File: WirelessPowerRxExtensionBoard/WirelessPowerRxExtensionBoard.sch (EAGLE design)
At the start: 37 parts, among them Q1 MOSFET-N, Q2 MOSFET-N, Q3 MOSFET-N

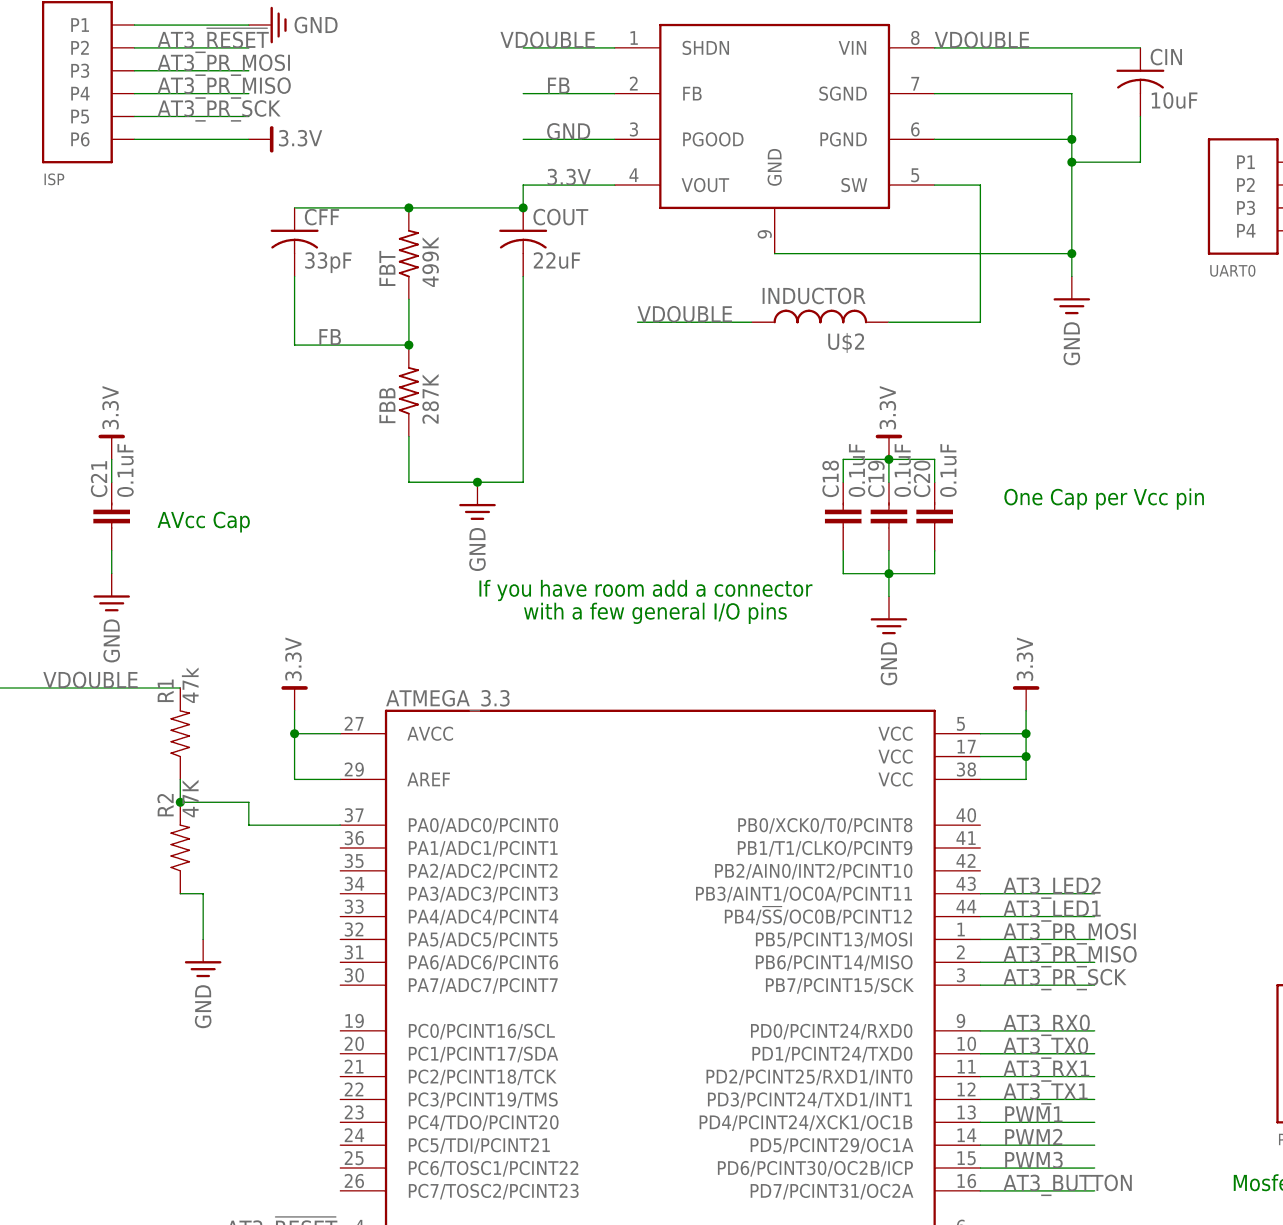
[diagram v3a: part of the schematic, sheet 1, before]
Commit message: Second Rerouting Revision Complete
Extended Ground plane across entire board, switched Voltage regulator
feedback resistors to 0603
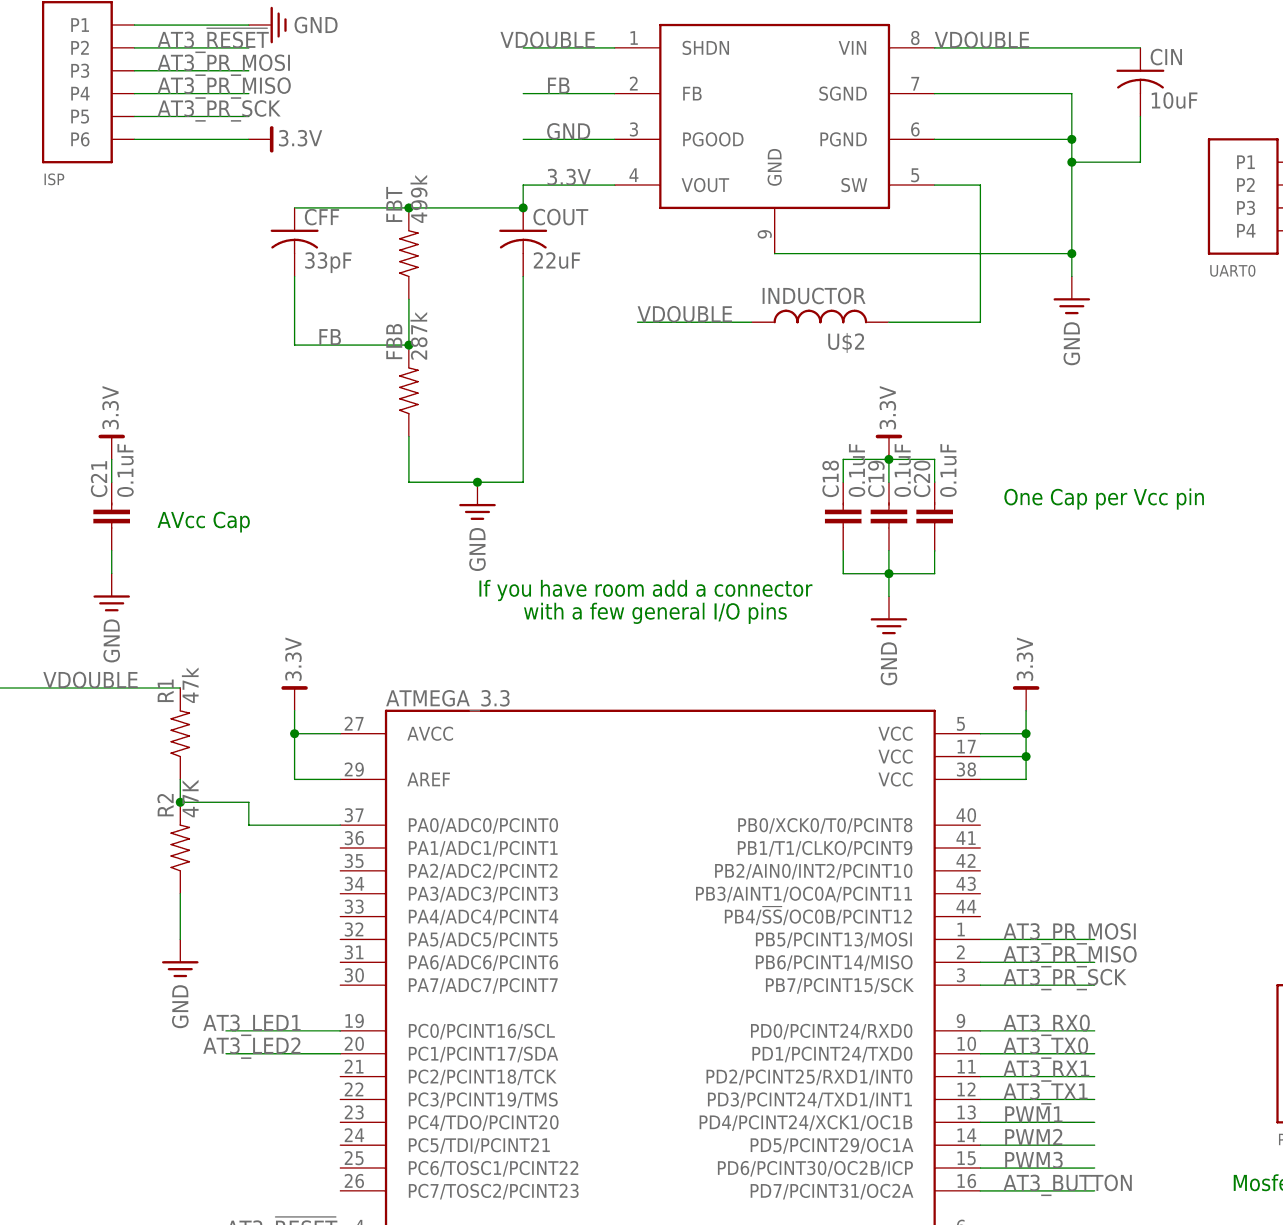
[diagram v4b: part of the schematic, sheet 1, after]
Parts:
- FBB: value 287K -> 287k; device resistor:R-US_M0805 -> carrick:RES0603
- FBT: value 499K -> 499k; device resistor:R-US_M0805 -> carrick:RES0603
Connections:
- net AT3_LED1: now also ATMEGA_3.3.PC0/PCINT16/SCL; no longer ATMEGA_3.3.PB4/!SS!/OC0B/PCINT12
- net AT3_LED2: now also ATMEGA_3.3.PC1/PCINT17/SDA; no longer ATMEGA_3.3.PB3/AINT1/OC0A/PCINT11
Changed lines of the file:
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@@
 <part name="CIN" library="rcl" deviceset="C-US" device="C0805" value="10uF"/>
 <part name="COUT" library="rcl" deviceset="C-US" device="C0805" value="22uF"/>
-<part name="FBT" library="resistor" deviceset="R-US_" device="M0805" value="499K"/>
-<part name="FBB" library="resistor" deviceset="R-US_" device="M0805" value="287K"/>
 <part name="SUPPLY3" library="000_carrick" deviceset="GND" device=""/>
 <part name="CFF" library="rcl" deviceset="C-US" device="C0201" value="33pF"/>
@@
 <part name="R1" library="carrick" deviceset="RES" device="0603" value="47k"/>
 <part name="R2" library="carrick" deviceset="RES" device="0603" value="47K"/>
+<part name="FBT" library="carrick" deviceset="RES" device="0603" value="499k"/>
+<part name="FBB" library="carrick" deviceset="RES" device="0603" value="287k"/>
 </parts>
 <sheets>
@@
 <instance part="CIN" gate="G$1" x="134.62" y="170.18"/>
 <instance part="COUT" gate="G$1" x="66.04" y="152.4"/>
-<instance part="FBT" gate="G$1" x="53.34" y="149.86" rot="R90"/>
-<instance part="FBB" gate="G$1" x="53.34" y="134.62" rot="R90"/>
 <instance part="SUPPLY3" gate="GND" x="60.96" y="121.92"/>
 <instance part="CFF" gate="G$1" x="40.64" y="152.4"/>
 <instance part="U$1" gate="G$1" x="93.98" y="165.1"/>
 <instance part="U$2" gate="G$1" x="99.06" y="142.24" rot="R90"/>
-<instance part="SUPPLY4" gate="GND" x="30.48" y="71.12"/>
+<instance part="SUPPLY4" gate="GND" x="27.94" y="71.12"/>
 <instance part="C1" gate="G$1" x="22.86" y="33.02"/>
 <instance part="C2" gate="G$1" x="22.86" y="17.78"/>
@@
 <instance part="R1" gate="G$1" x="27.94" y="96.52" rot="R90"/>
 <instance part="R2" gate="G$1" x="27.94" y="83.82" rot="R90"/>
+<instance part="FBT" gate="G$1" x="53.34" y="149.86" rot="R90"/>
+<instance part="FBB" gate="G$1" x="53.34" y="134.62" rot="R90"/>
 </instances>
 <busses>
@@
 <pinref part="COUT" gate="G$1" pin="2"/>
 <wire x1="66.04" y1="147.32" x2="66.04" y2="124.46" width="0.1524" layer="91"/>
-<pinref part="FBB" gate="G$1" pin="1"/>
 <wire x1="66.04" y1="124.46" x2="60.96" y2="124.46" width="0.1524" layer="91"/>
 <wire x1="60.96" y1="124.46" x2="53.34" y2="124.46" width="0.1524" layer="91"/>
@@
 <pinref part="SUPPLY3" gate="GND" pin="GND"/>
 <junction x="60.96" y="124.46"/>
+<pinref part="FBB" gate="G$1" pin="1"/>
 </segment>
 <segment>
 <pinref part="SUPPLY4" gate="GND" pin="GND"/>
 <pinref part="R2" gate="G$1" pin="1"/>
-<wire x1="27.94" y1="78.74" x2="30.48" y2="78.74" width="0.1524" layer="91"/>
-<wire x1="30.48" y1="78.74" x2="30.48" y2="73.66" width="0.1524" layer="91"/>
+<wire x1="27.94" y1="73.66" x2="27.94" y2="78.74" width="0.1524" layer="91"/>
 </segment>
 </net>
@@
 <pinref part="COUT" gate="G$1" pin="1"/>
 <wire x1="66.04" y1="157.48" x2="66.04" y2="154.94" width="0.1524" layer="91"/>
-<pinref part="FBT" gate="G$1" pin="2"/>
-<wire x1="66.04" y1="154.94" x2="53.34" y2="154.94" width="0.1524" layer="91"/>
 <junction x="66.04" y="154.94"/>
 <pinref part="CFF" gate="G$1" pin="1"/>
+<wire x1="66.04" y1="154.94" x2="53.34" y2="154.94" width="0.1524" layer="91"/>
+<pinref part="U$1" gate="G$1" pin="VOUT"/>
+<pinref part="FBT" gate="G$1" pin="2"/>
 <wire x1="53.34" y1="154.94" x2="40.64" y2="154.94" width="0.1524" layer="91"/>
 <junction x="53.34" y="154.94"/>
-<pinref part="U$1" gate="G$1" pin="VOUT"/>
 </segment>
 </net>
@@
 </segment>
 <segment>
-<wire x1="129.54" y1="76.2" x2="116.84" y2="76.2" width="0.1524" layer="91"/>
-<label x="119.38" y="76.2" size="1.778" layer="95"/>
-<pinref part="ATMEGA_3.3" gate="G$1" pin="PB4/!SS!/OC0B/PCINT12"/>
+<pinref part="ATMEGA_3.3" gate="G$1" pin="PC0/PCINT16/SCL"/>
+<wire x1="45.72" y1="63.5" x2="33.02" y2="63.5" width="0.1524" layer="91"/>
+<label x="30.48" y="63.5" size="1.778" layer="95"/>
 </segment>
 </net>
@@
 </segment>
 <segment>
-<wire x1="129.54" y1="78.74" x2="116.84" y2="78.74" width="0.1524" layer="91"/>
-<label x="119.38" y="78.74" size="1.778" layer="95"/>
-<pinref part="ATMEGA_3.3" gate="G$1" pin="PB3/AINT1/OC0A/PCINT11"/>
+<pinref part="ATMEGA_3.3" gate="G$1" pin="PC1/PCINT17/SDA"/>
+<wire x1="45.72" y1="60.96" x2="33.02" y2="60.96" width="0.1524" layer="91"/>
+<label x="30.48" y="60.96" size="1.778" layer="95"/>
 </segment>
 </net>
@@
 <segment>
 <wire x1="40.64" y1="147.32" x2="40.64" y2="139.7" width="0.1524" layer="91"/>
-<pinref part="FBB" gate="G$1" pin="2"/>
 <wire x1="40.64" y1="139.7" x2="53.34" y2="139.7" width="0.1524" layer="91"/>
-<pinref part="FBT" gate="G$1" pin="1"/>
 <wire x1="53.34" y1="144.78" x2="53.34" y2="139.7" width="0.1524" layer="91"/>
-<junction x="53.34" y="139.7"/>
 <pinref part="CFF" gate="G$1" pin="2"/>
 <label x="43.18" y="139.7" size="1.778" layer="95"/>
-</segment>
-</net>
+<pinref part="FBT" gate="G$1" pin="1"/>
+<pinref part="FBB" gate="G$1" pin="2"/>
+<junction x="53.34" y="139.7"/>
+</segment>
+</net>
